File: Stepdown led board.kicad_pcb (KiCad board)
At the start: 2 copper layers, 58.4 x 12.7 mm, 5 parts, among them J1 IN, J2 OUT, J3 Stepdown module

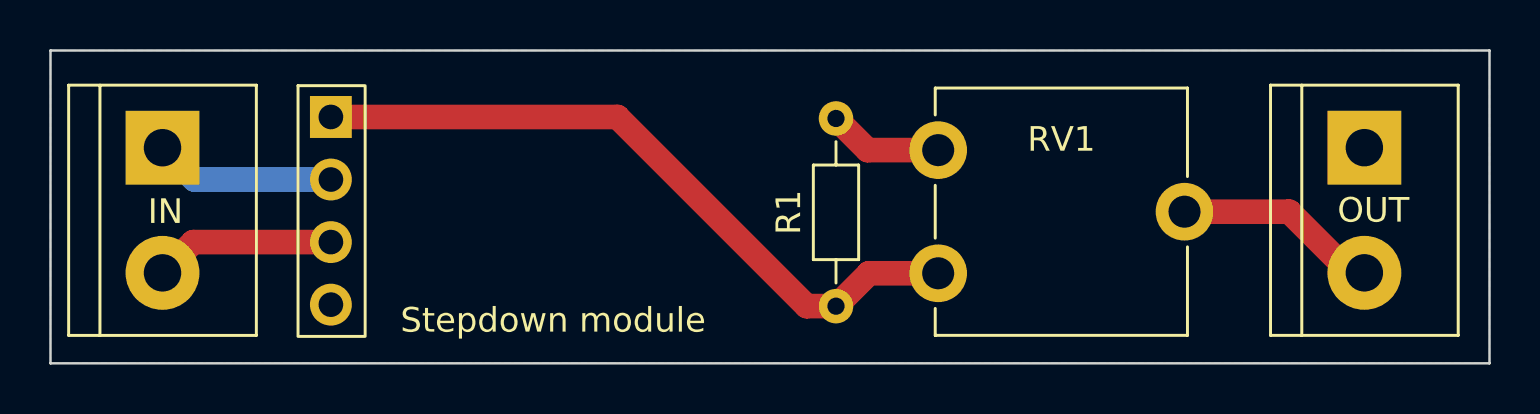
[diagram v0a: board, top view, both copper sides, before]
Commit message: - Fixed dumb stepdown module inversion - Fixed Front silkscreen
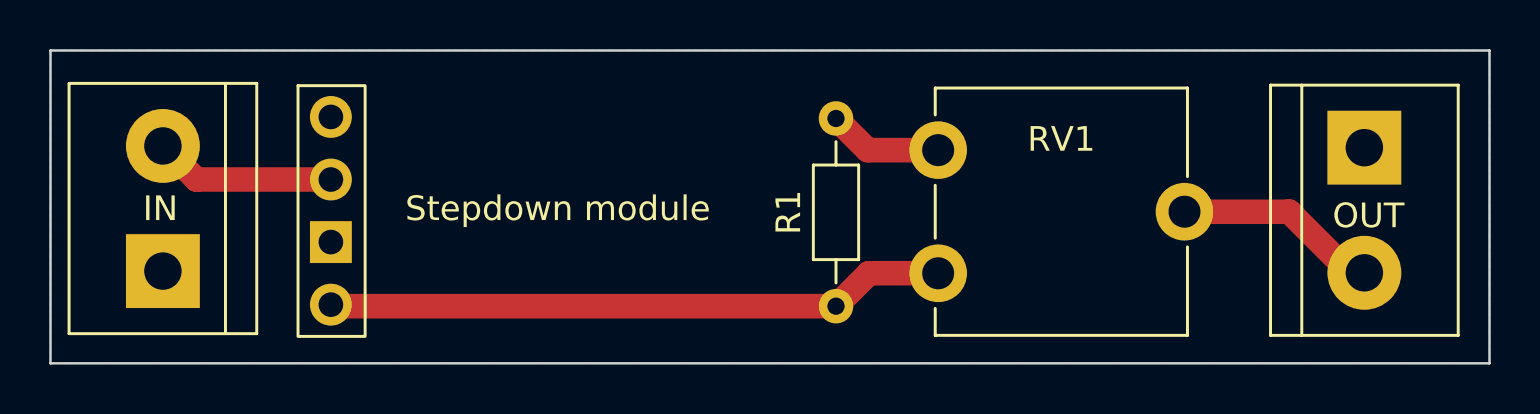
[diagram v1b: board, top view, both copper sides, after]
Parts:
- IN: renamed from J1; value IN -> J1
- OUT: renamed from J2; value OUT -> J2
- Stepdown module: renamed from J3; value Stepdown module -> J3
- moved IN 5.01 mm to (24.9, 31.8), turned to 90 degrees
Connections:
- Stepdown module pad 1: Vout -> unconnected-(J3-Pad1)
- Stepdown module pad 2: GND -> +12V
- Stepdown module pad 3: +12V -> GND
- Stepdown module pad 4: unconnected-(J3-Pad4) -> Vout
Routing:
- net GND: track 7.37 -> 0.00 mm
- net Vout: track 28.4 -> 25.2 mm
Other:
- board text added: "v1.0.1"
- board text removed: "v1.0"
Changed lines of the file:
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@@
       (drillshape 0)
       (scaleselection 1)
-      (outputdirectory "Gerbers/")
+      (outputdirectory "jlcpcb/V1.0.1/")
     )
   )
@@
   (net 3 "Vled")
   (net 4 "Vout")
-  (net 5 "unconnected-(J3-Pad4)")
+  (net 5 "unconnected-(J3-Pad1)")
   (net 6 "Net-(R1-Pad2)")
   (footprint "Connector_PinHeader_2.54mm:PinHeader_1x04_P2.54mm_Vertical" (layer "F.Cu")
@@
     (property "Sheetname" "")
     (attr through_hole)
-    (fp_text reference "J3" (at 3.045838 4.026773) (layer "F.SilkS") hide
-      (effects (font (size 1 1) (thickness 0.15)))
-    )
-    (fp_text value "Stepdown module" (at 9.022001 8.252344) (layer "F.SilkS")
+    (fp_text reference "Stepdown module" (at 9.213373 3.722398) (layer "F.SilkS")
+      (effects (font (size 1 1) (thickness 0.15)))
+    )
+    (fp_text value "J3" (at 9.022001 8.252344) (layer "F.SilkS") hide
       (effects (font (size 1 1) (thickness 0.15)))
     )
@@
     (fp_line (start -1.8 9.4) (end 1.8 9.4) (layer "F.CrtYd") (width 0.05))
     (fp_line (start -1.8 -1.8) (end -1.8 9.4) (layer "F.CrtYd") (width 0.05))
-    (pad "1" thru_hole rect (at 0 0) (size 1.7 1.7) (drill 1) (layers *.Cu *.Mask)
-      (net 4 "Vout") (pinfunction "Pin_1") (pintype "passive"))
+    (pad "1" thru_hole circle (at 0 0) (size 1.7 1.7) (drill 1) (layers *.Cu *.Mask)
+      (net 5 "unconnected-(J3-Pad1)") (pinfunction "Pin_1") (pintype "passive+no_connect"))
     (pad "2" thru_hole oval (at 0 2.54) (size 1.7 1.7) (drill 1) (layers *.Cu *.Mask)
-      (net 1 "GND") (pinfunction "Pin_2") (pintype "passive"))
-    (pad "3" thru_hole oval (at 0 5.08) (size 1.7 1.7) (drill 1) (layers *.Cu *.Mask)
-      (net 2 "+12V") (pinfunction "Pin_3") (pintype "passive"))
+      (net 2 "+12V") (pinfunction "Pin_2") (pintype "passive"))
+    (pad "3" thru_hole rect (at 0 5.08) (size 1.7 1.7) (drill 1) (layers *.Cu *.Mask)
+      (net 1 "GND") (pinfunction "Pin_3") (pintype "passive"))
     (pad "4" thru_hole oval (at 0 7.62) (size 1.7 1.7) (drill 1) (layers *.Cu *.Mask)
-      (net 5 "unconnected-(J3-Pad4)") (pinfunction "Pin_4") (pintype "passive+no_connect"))
+      (net 4 "Vout") (pinfunction "Pin_4") (pintype "passive"))
     (model "${KICAD6_3DMODEL_DIR}/Connector_PinHeader_2.54mm.3dshapes/PinHeader_1x04_P2.54mm_Vertical.wrl"
       (offset (xyz 0 0 0))
@@
     (property "Sheetname" "")
     (attr through_hole)
-    (fp_text reference "J2" (at -1.396947 -2.65771 180) (layer "F.SilkS") hide
-      (effects (font (size 1 1) (thickness 0.15)))
-    )
-    (fp_text value "OUT" (at 2.54 -0.363829 180) (layer "F.SilkS")
+    (fp_text reference "OUT" (at 2.765119 -0.163348 180) (layer "F.SilkS")
+      (effects (font (size 1 1) (thickness 0.15)))
+    )
+    (fp_text value "J2" (at 2.54 -0.363829 180) (layer "F.SilkS") hide
       (effects (font (size 1 1) (thickness 0.15)))
     )
@@
   )
   (footprint "TerminalBlock:TerminalBlock_bornier-2_P5.08mm" (layer "F.Cu")
-    (at 24.867173 26.807237 -90)
+    (at 24.88389 31.815187 90)
     (descr "simple 2-pin terminal block, pitch 5.08mm, revamped version of bornier2")
     (tags "terminal block bornier2")
@@
     (property "Sheetname" "")
     (attr through_hole)
-    (fp_text reference "J1" (at -1.393624 -2.713449 180) (layer "F.SilkS") hide
-      (effects (font (size 1 1) (thickness 0.15)))
-    )
-    (fp_text value "IN" (at 2.590485 -0.117741 180) (layer "F.SilkS")
-      (effects (font (size 1 1) (thickness 0.15)))
-    )
-    (fp_text user "${REFERENCE}" (at 2.879456 -2.496459 180) (layer "F.Fab") hide
+    (fp_text reference "IN" (at 2.534592 -0.10127) (layer "F.SilkS")
+      (effects (font (size 1 1) (thickness 0.15)))
+    )
+    (fp_text value "J1" (at 2.590485 -0.117741) (layer "F.SilkS") hide
+      (effects (font (size 1 1) (thickness 0.15)))
+    )
+    (fp_text user "${REFERENCE}" (at 2.879456 -2.496459) (layer "F.Fab") hide
       (effects (font (size 1 1) (thickness 0.15)))
     )
@@
     (fp_line (start 7.54 -3.75) (end -2.46 -3.75) (layer "F.Fab") (width 0.1))
     (fp_line (start -2.46 -3.75) (end -2.46 3.75) (layer "F.Fab") (width 0.1))
-    (pad "1" thru_hole rect (at 0 0 270) (size 3 3) (drill 1.52) (layers *.Cu *.Mask)
+    (pad "1" thru_hole rect (at 0 0 90) (size 3 3) (drill 1.52) (layers *.Cu *.Mask)
       (net 1 "GND") (pinfunction "Pin_1") (pintype "passive"))
-    (pad "2" thru_hole circle (at 5.08 0 270) (size 3 3) (drill 1.52) (layers *.Cu *.Mask)
+    (pad "2" thru_hole circle (at 5.08 0 90) (size 3 3) (drill 1.52) (layers *.Cu *.Mask)
       (net 2 "+12V") (pinfunction "Pin_2") (pintype "passive"))
     (model "${KICAD6_3DMODEL_DIR}/TerminalBlock.3dshapes/TerminalBlock_bornier-2_P5.08mm.wrl"
@@
   (gr_rect (start 29.379071 23) (end 48.949597 35.406103) (layer "F.Mask") (width 0.2) (fill none))
   (gr_rect (start 20.32 22.86) (end 78.74 35.56) (layer "Edge.Cuts") (width 0.1) (fill none))
-  (gr_text "v1.0" (at 76.349599 34.3104) (layer "B.SilkS")
+  (gr_text "v1.0.1" (at 75.889012 34.395676) (layer "B.SilkS")
     (effects (font (size 1 1) (thickness 0.15)) (justify mirror))
   )
-  (segment (start 31.703356 28.098197) (end 26.158133 28.098197) (width 1) (layer "B.Cu") (net 1))
-  (segment (start 26.158133 28.098197) (end 24.867173 26.807237) (width 1) (layer "B.Cu") (net 1))
-  (segment (start 31.703356 30.638197) (end 26.116213 30.638197) (width 1) (layer "F.Cu") (net 2))
-  (segment (start 26.116213 30.638197) (end 24.867173 31.887237) (width 1) (layer "F.Cu") (net 2))
+  (segment (start 31.703356 28.098197) (end 26.2469 28.098197) (width 1) (layer "F.Cu") (net 2))
+  (segment (start 26.2469 28.098197) (end 24.88389 26.735187) (width 1) (layer "F.Cu") (net 2))
   (segment (start 70.613191 29.404773) (end 73.094076 31.885658) (width 1) (layer "F.Cu") (net 3))
   (segment (start 66.35799 29.404773) (end 70.613191 29.404773) (width 1) (layer "F.Cu") (net 3))
+  (segment (start 52.209295 33.239773) (end 31.764932 33.239773) (width 1) (layer "F.Cu") (net 4))
+  (segment (start 31.764932 33.239773) (end 31.703356 33.178197) (width 1) (layer "F.Cu") (net 4))
   (segment (start 56.35799 31.904773) (end 53.544295 31.904773) (width 1) (layer "F.Cu") (net 4))
-  (segment (start 51.019773 33.239773) (end 52.209295 33.239773) (width 1) (layer "F.Cu") (net 4))
-  (segment (start 43.338197 25.558197) (end 51.019773 33.239773) (width 1) (layer "F.Cu") (net 4))
-  (segment (start 31.703356 25.558197) (end 43.338197 25.558197) (width 1) (layer "F.Cu") (net 4))
   (segment (start 53.544295 31.904773) (end 52.209295 33.239773) (width 1) (layer "F.Cu") (net 4))
   (segment (start 53.494295 26.904773) (end 52.209295 25.619773) (width 1) (layer "F.Cu") (net 6))
